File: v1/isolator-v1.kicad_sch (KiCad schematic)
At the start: 39 parts, among them J1 HOST, J2 PORT, T1 750313638, U1 ADuM4165, U2 USBLC6-2SC6, U3 USBLC6-2SC6, U4 SN6505BDBV, U5 TLV76750DGNR, U6 TPS2553DBV, Y1 24M 8pF

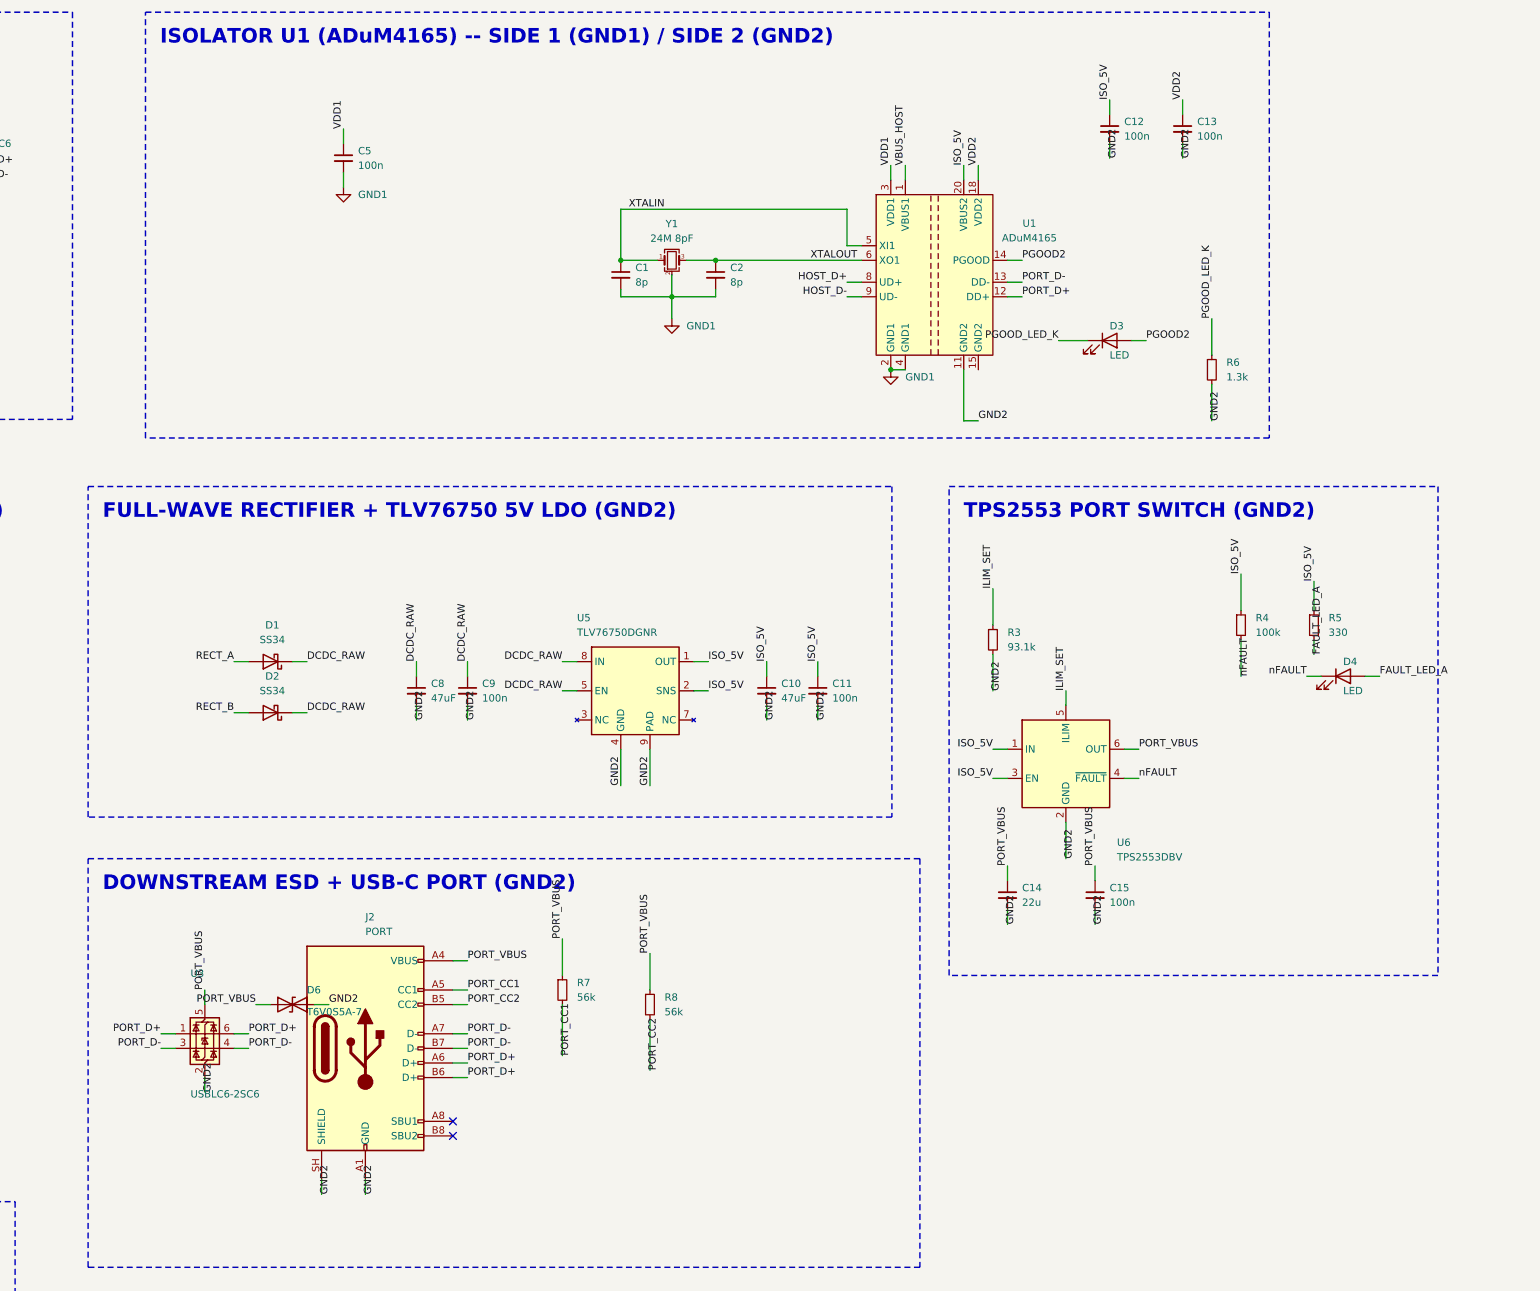
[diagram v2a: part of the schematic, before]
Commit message: fix(v1/sch): Task 5 review round 1 - PGOOD buffer via 2N7002, layout overlaps
Important: the "PGOOD is push-pull, direct-drive the LED" conclusion didn't
hold up - absence of a VOH/VOL spec and no pull-up in the datasheet's block
diagram is not evidence of push-pull, and v2's own schematic already drives
this identical PGOOD2 signal through a 2N7002 (Q2) with a 100k pull-up to
its isolated 3.3V rail and a 100k pull-down, not a direct LED drive.

Replicated that arrangement: Q1 (2N7002) buffers PGOOD2, R9 (100k) pulls
the gate up to VDD2 - never ISO_5V, since the ADuM4165 abs-max on PGOOD is
VDD2+0.5V (Table 8) and a 5V pull-up would exceed it if the pin is actually
open-drain - and R10 (100k) pulls it down to GND2, matching v2's R25/R26
pair. D3 now runs off ISO_5V through Q1's drain; recomputed its series
resistor for the 5V rail (was 1.3k sized for 3.3V): (5.0-2.0V)/1mA=3kOhm,
nearest E96 3.01k, giving ~0.996mA. R9 adding ~33uA to VDD2 is correct per
the reviewer's read of the capacitance-only "nothing else on VDD2" rule,
not a violation - documented explicitly for the next reviewer.

Also fixes three (plus two more of the same class found while rebuilding
the PGOOD row) text-overlap layout bugs, all traced to the same root
cause: KiCad's net-label justify "left top" on a rotation-90 label grows
the text back toward the originating component, not away from it, which
Task 4's original labels never exposed because they always had empty
space to grow into. Confirmed the correct direction ("right bottom") by
direct A/B render comparison, not just re-reading coordinates.

Embedded the 2N7002 symbol via this project's own isolator-lib.kicad_sym
(matching the TPS2553DBV/750313638/TLV76750DGNR pattern) rather than the
stock Transistor_FET library, to avoid reproducing the exact
extends-vs-flattened lib_symbol_mismatch Task 4 already investigated and
found unfixable without breaking connectivity - holds the ERC baseline at
exactly one pre-existing warning.

ERC: 0 errors, 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
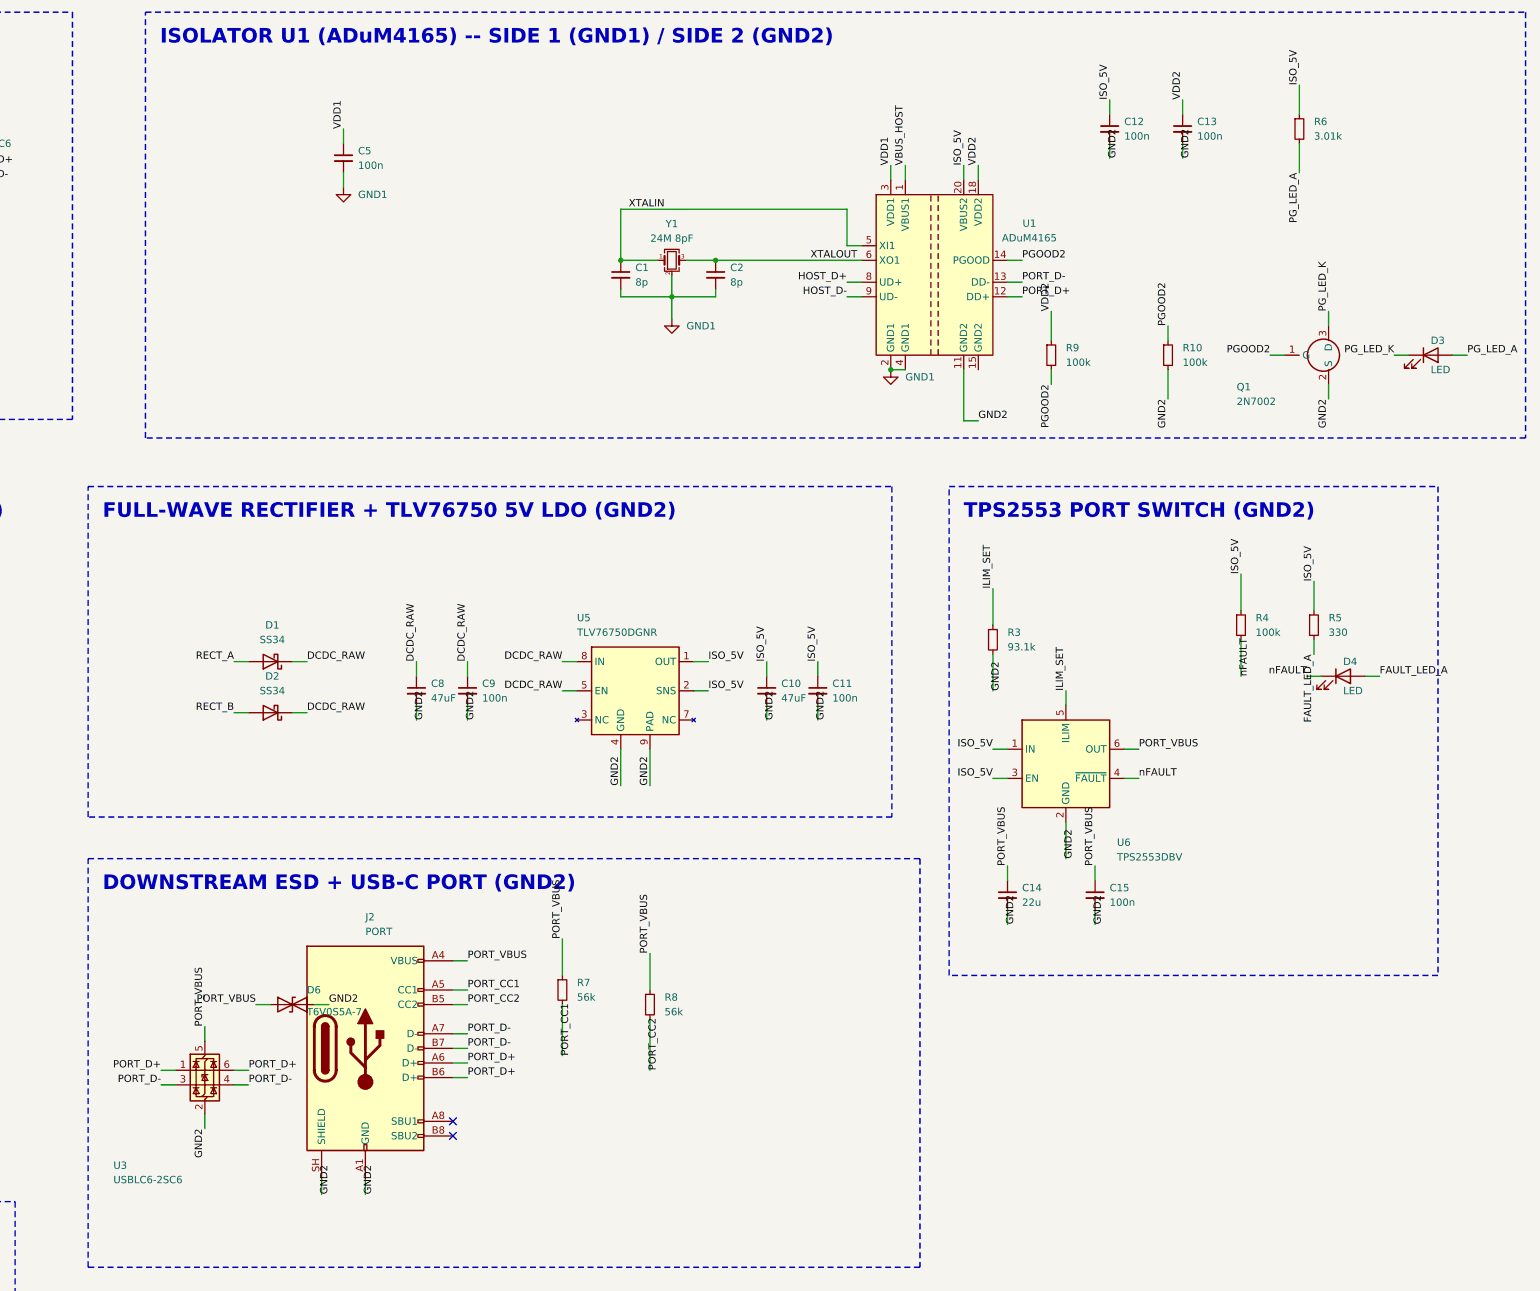
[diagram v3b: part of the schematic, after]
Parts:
- added Q1: 2N7002, Package_TO_SOT_SMD:SOT-23, symbol isolator-lib:2N7002
- added R10, R9: 100k, Resistor_SMD:R_0603_1608Metric, symbol Device:R_Small
- R6: value 1.3k -> 3.01k; MPN RC0603FR-071K3L -> RC0603FR-073K01L
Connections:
- net GND2: now also Q1.2 (S), R10.2; no longer R6.2
- net ISO_5V: now also R6.1
- net PGOOD2: now also Q1.1 (G), R10.1, R9.2; no longer D3.2 (A)
- net VDD2: now also R9.1
- net PGOOD_LED_K renamed PG_LED_K
- net PG_LED_K: now also Q1.3 (D); no longer R6.1
- new net PG_LED_A: D3.2 (A), R6.2

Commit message: fix(v1): Task 5 review round 2 - PGOOD confirmed push-pull, remove R9/R10, fix 4 label overlaps
PGOOD structure resolved from primary evidence rather than left as a hedge: ADI's own
EVAL-ADuM4165EBZ/EVAL-ADuM4166EBZ schematics and BOMs (datasheets/eval-adum4165-4166-ug-2027.pdf,
Figure 3/6 + Table 4/5) wire PGOOD straight to a test header with zero external resistors on
either board, and the pin description (adum4165-4166.pdf Table 12/13) describes "high output"/
"low output" states, not open-drain release. Push-pull confirmed -> removed R9 (pull-up) and R10
(pull-down), the indeterminate bias divider on Q1's gate; Q1 itself is kept as a level-shifting
buffer for the 5V-domain LED drive. VDD2 net is now exactly {C13.1, U1.18} again.

Also fixed 3 flagged net-label text overlaps (R7 PORT_VBUS vs box title; U3/D6 PORT_VBUS-vs-
PORT_VBUS stack; the VDD2/PORT_D+ collision, resolved automatically by the R9 removal) plus one
more (nFAULT vs FAULT_LED_A) caught by a full-schematic programmatic overlap sweep. Verified both
programmatically (0 candidate overlaps across 114 label/text items) and visually (re-rendered SVG
at 6000px, inspected each region).

ERC baseline held: 0 errors, exactly 1 pre-existing lib_symbol_mismatch warning on U4.

Co-Authored-By: Claude Opus 5 <noreply@anthropic.com>
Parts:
- removed R10, R9: 100k, Resistor_SMD:R_0603_1608Metric, symbol Device:R_Small

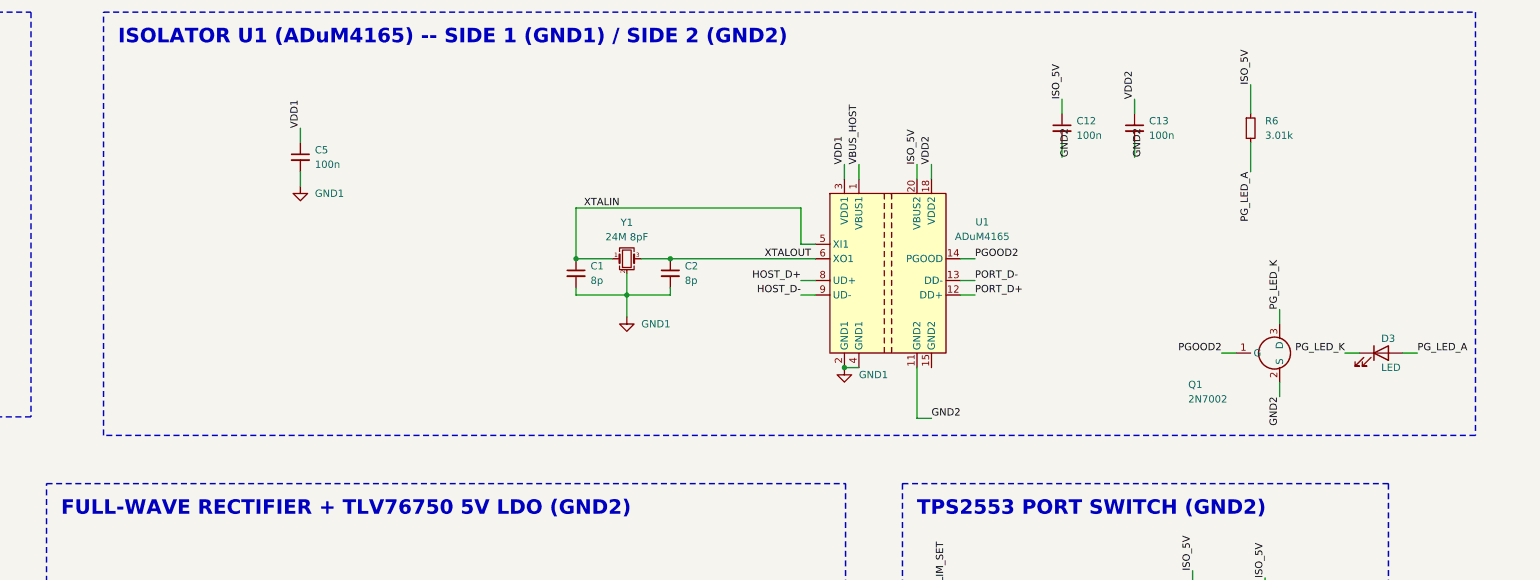
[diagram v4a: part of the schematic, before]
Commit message: fix(v1): Task 5 review round 3 - PGOOD reclassified unspecified, restore R9 (DNP)/R10 (populated)
Independent review found the eval-board evidence has no differential power: VDD1/VBUS1 (LDO
power rails, unambiguously not open-drain-relevant) route to unpopulated DNI test headers the
identical way PGOOD does, and Table 3 of the eval guide confirms this is the generic convention
for all nine test points regardless of pin type. The "high output/low output" pin-description
language doesn't distinguish push-pull from open-drain either. PGOOD reclassified from "confirmed
push-pull" to "unspecified" -> implemented the brief's third case:

- R10 restored: 100k, PGOOD2 -> GND2, POPULATED. Gate parks low (Q1 definitively OFF) if PGOOD is
  open-drain; negligible ~33uA load if push-pull.
- R9 restored: 100k, PGOOD2 -> VDD2 (never ISO_5V, abs-max V_DD2+0.5V), marked DNP (dnp yes,
  in_bom no) so it never populates alongside R10.
- Added a schematic text note documenting the DNP/populate convention for bring-up.
- Relocated R9 10.16mm right (x=332.74 -> 342.9) to avoid re-triggering the VDD2-vs-PORT_D+ label
  collision that R9's return reintroduced at its original position; shortened R9's Value field
  ("100k DNP" -> "100k") after it collided with R10's own reference text.
- Extended the "ISOLATOR U1" section box bottom (91.8845 -> 99.06mm) to fit the note without
  touching neighboring section boxes.

Also corrected a wrong round-2 claim (in the report only, isolator.kicad_sch untouched): v2's
PGOOD2 net has a third functional consumer, U4.27 (USB2514B VBUS_DET), that v1's PGOOD2 does not
have, so v1's R9/R10 removal reasoning does not transfer to v2's R25/R26.

Verified: ERC clean (0 errors, 1 pre-existing lib_symbol_mismatch on U4), netlist probes match,
isolation check clean, full-schematic label-overlap sweep 0/119 candidates + visual re-confirmation.

Co-Authored-By: Claude Opus 5 <noreply@anthropic.com>
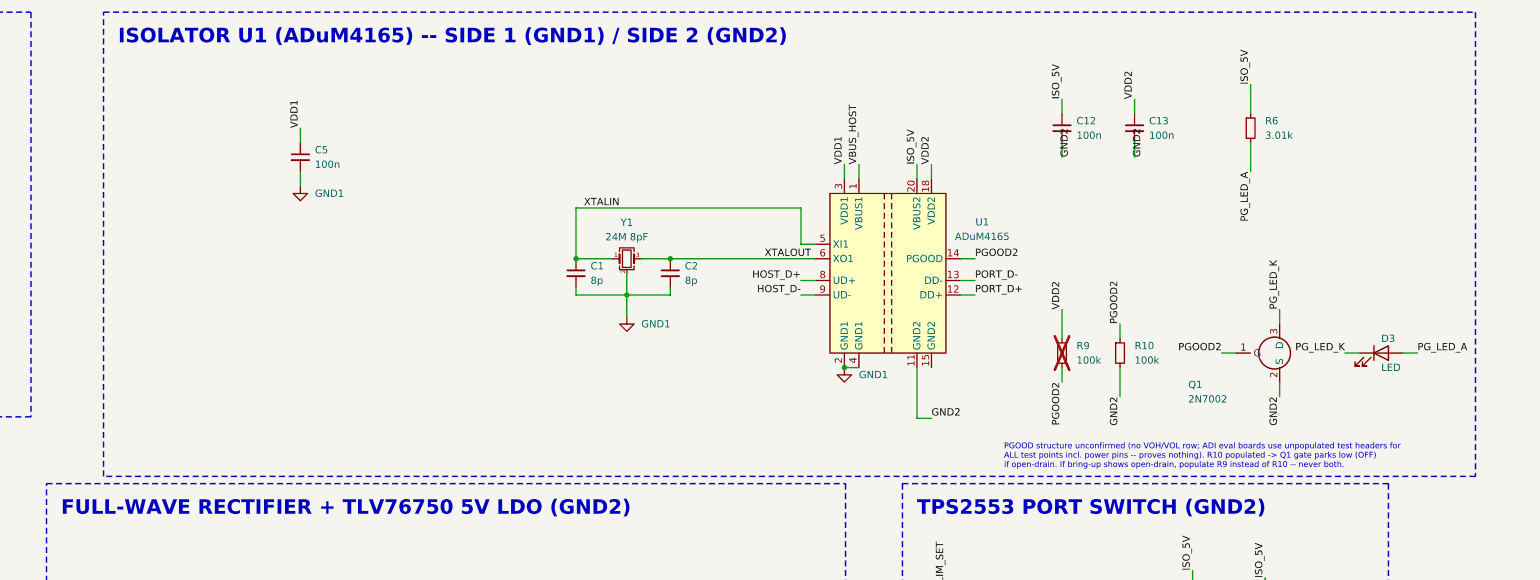
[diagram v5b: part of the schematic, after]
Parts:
- added R10, R9: 100k, Resistor_SMD:R_0603_1608Metric, symbol Device:R_Small
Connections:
- net GND2: now also R10.2
- net PGOOD2: now also R10.1, R9.2
- net VDD2: now also R9.1
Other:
- note added: "PGOOD structure unconfirmed (no VOH/VOL row; ADI eval boards use unpopulated test headers for ALL test points incl. power pins -- proves nothing). R10 populated -> Q1 gate parks low (OFF) if open-drain. If bring-up shows open-drain, populate R9 instead of R10 -- never both."
